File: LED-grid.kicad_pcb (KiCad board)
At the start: 2 copper layers, 75 x 75 mm, 301 parts

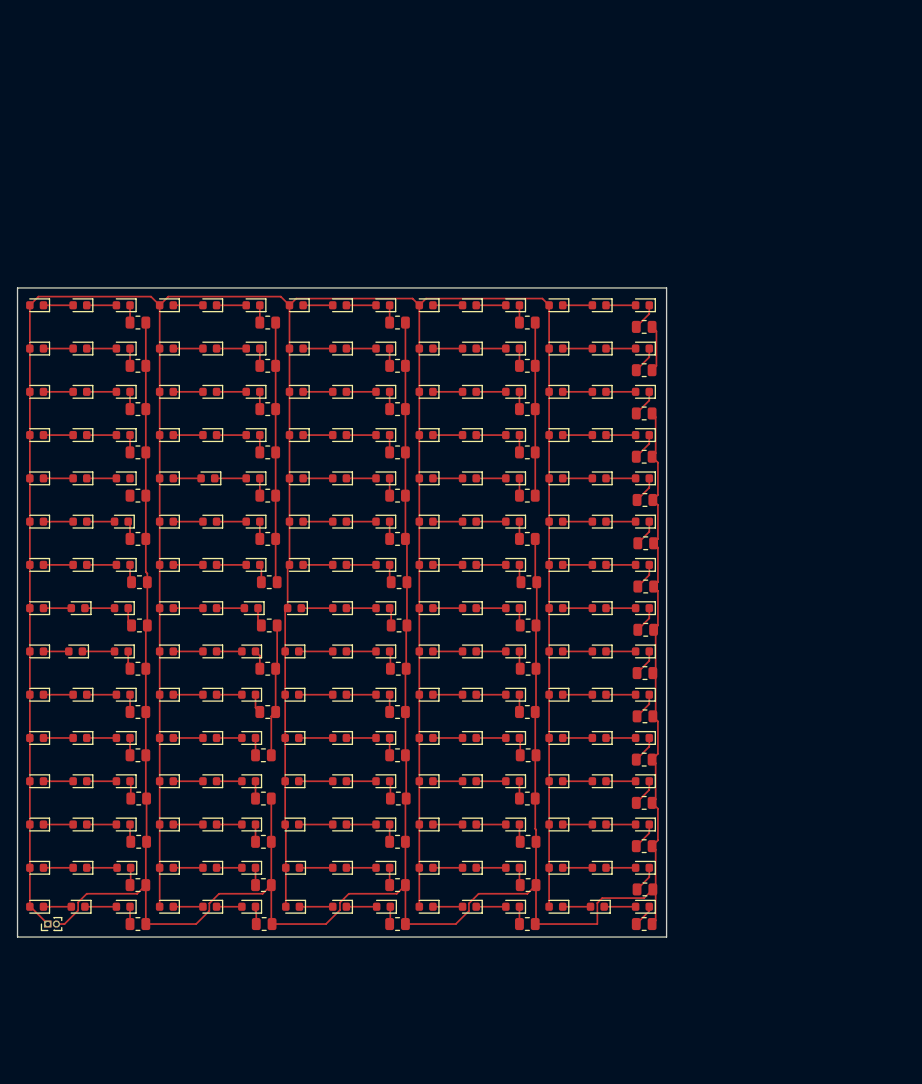
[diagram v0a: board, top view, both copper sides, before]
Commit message: Version 1.0.1 We can now actually control the brightness using a potentiometer
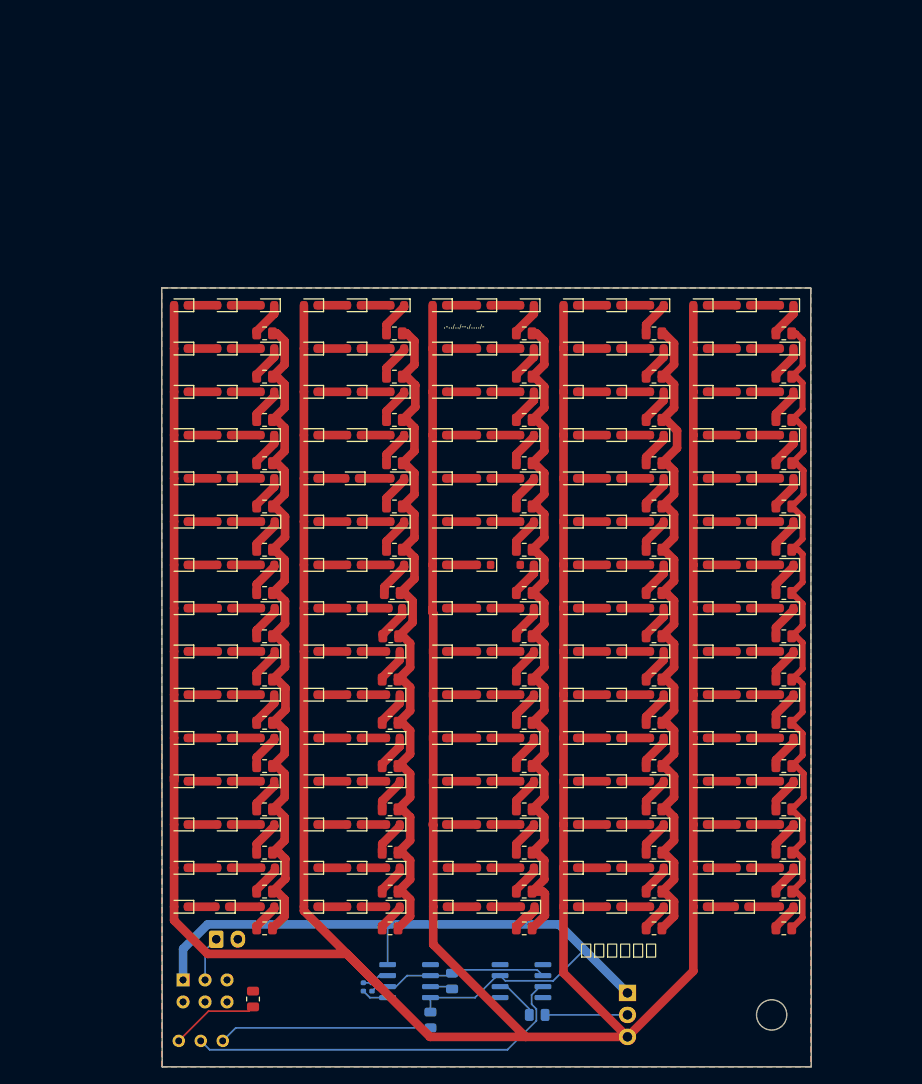
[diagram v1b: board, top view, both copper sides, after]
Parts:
- added C1: 100n, Capacitor_SMD:C_0402_1005Metric, B.Cu at (153.2, 135.8)
- added C2: 100n, Capacitor_SMD:C_0402_1005Metric, B.Cu at (154.2, 135.8)
- added G***: LOGO, SFH11_PBPC_D10_ST_BK:GoblinCatLogo, B.Cu at (139.5, 66.2)
- added G***: LOGO, SFH11_PBPC_D10_ST_BK:PiShockLogo, B.Cu at (190.5, 115.0)
- added Q1: NMOS, Package_TO_SOT_THT:TO-220-3_Horizontal_TabUp, B.Cu at (183.8, 136.5)
- added R76: 1k, Resistor_SMD:R_0805_2012Metric, B.Cu at (163.5, 135.1)
- added R77: 1k, Resistor_SMD:R_0805_2012Metric, B.Cu at (161.0, 139.6)
- added R78: 1k, Resistor_SMD:R_0805_2012Metric, F.Cu at (140.5, 137.2)
- added R79: 1k, Resistor_SMD:R_0805_2012Metric, B.Cu at (173.3, 139.0)
- added RV1: 3296X-1-102LF, Potentiometer_THT:Potentiometer_Bourns_3296X_Horizontal, B.Cu at (137.0, 142.0)
- added SW1: SW_Wuerth_450301014042, Button_Switch_THT:SW_NKK_G1xJP, B.Cu at (132.4, 135.0)
- added U1: NE555D, Package_SO:SOIC-8_3.9x4.9mm_P1.27mm, B.Cu at (158.5, 135.1)
- added U2: LM741, Package_SO:SOIC-8_3.9x4.9mm_P1.27mm, B.Cu at (171.5, 135.1)
- BT1: footprint Connector_PinHeader_1.00mm:PinHeader_1x02_P1.00mm_Vertical -> Connector_JST:JST_EH_B2B-EH-A_1x02_P2.50mm_Vertical; moved to B.Cu
- moved BT1 19.5 mm to (136.2, 130.2), turned to 0 degrees
- moved D122 17.2 mm to (137.2, 97.0)
- moved D202 17.0 mm to (162.1, 122.0)
- moved D217 17.0 mm to (162.1, 126.5)
- moved D127 17.0 mm to (162.0, 97.0)
- moved D142 17.0 mm to (162.0, 102.0)
- moved D157 17.0 mm to (162.0, 107.0)
- moved D172 17.0 mm to (162.0, 112.0)
- moved D187 17.0 mm to (162.0, 117.0)
- moved D107 16.9 mm to (137.2, 92.0)
- moved D108 16.9 mm to (142.2, 92.0)
- moved D123 16.9 mm to (142.2, 97.0)
- moved D78 16.9 mm to (142.2, 82.0)
- moved D112 16.8 mm to (162.0, 92.0)
- moved D111 16.7 mm to (157.0, 92.0)
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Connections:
- BT1 pad 1: VCC -> Net-(BT1-+)
- D1 pad 2: VCC -> LED_PWR
- D10 pad 2: VCC -> LED_PWR
- D100 pad 2: VCC -> LED_PWR
- D103 pad 2: VCC -> LED_PWR
- D106 pad 2: VCC -> LED_PWR
- D109 pad 2: VCC -> LED_PWR
- D112 pad 2: VCC -> LED_PWR
- D115 pad 2: VCC -> LED_PWR
- D118 pad 2: VCC -> LED_PWR
- D121 pad 2: VCC -> LED_PWR
- D124 pad 2: VCC -> LED_PWR
- D127 pad 2: VCC -> LED_PWR
- D13 pad 2: VCC -> LED_PWR
- D130 pad 2: VCC -> LED_PWR
- D133 pad 2: VCC -> LED_PWR
- D136 pad 2: VCC -> LED_PWR
- D139 pad 2: VCC -> LED_PWR
- D142 pad 2: VCC -> LED_PWR
- D145 pad 2: VCC -> LED_PWR
- D148 pad 2: VCC -> LED_PWR
- D151 pad 2: VCC -> LED_PWR
- D154 pad 2: VCC -> LED_PWR
- D157 pad 2: VCC -> LED_PWR
- D16 pad 2: VCC -> LED_PWR
- D160 pad 2: VCC -> LED_PWR
- D163 pad 2: VCC -> LED_PWR
- D166 pad 2: VCC -> LED_PWR
- D169 pad 2: VCC -> LED_PWR
- D172 pad 2: VCC -> LED_PWR
- D175 pad 2: VCC -> LED_PWR
- D178 pad 2: VCC -> LED_PWR
- D181 pad 2: VCC -> LED_PWR
- D184 pad 2: VCC -> LED_PWR
- D187 pad 2: VCC -> LED_PWR
- D19 pad 2: VCC -> LED_PWR
- D190 pad 2: VCC -> LED_PWR
- D193 pad 2: VCC -> LED_PWR
- D196 pad 2: VCC -> LED_PWR
- D199 pad 2: VCC -> LED_PWR
- D202 pad 2: VCC -> LED_PWR
- D205 pad 2: VCC -> LED_PWR
- D208 pad 2: VCC -> LED_PWR
- D211 pad 2: VCC -> LED_PWR
- D214 pad 2: VCC -> LED_PWR
- D217 pad 2: VCC -> LED_PWR
- D22 pad 2: VCC -> LED_PWR
- D220 pad 2: VCC -> LED_PWR
- D223 pad 2: VCC -> LED_PWR
- D25 pad 2: VCC -> LED_PWR
- D28 pad 2: VCC -> LED_PWR
- D31 pad 2: VCC -> LED_PWR
- D34 pad 2: VCC -> LED_PWR
- D37 pad 2: VCC -> LED_PWR
- D4 pad 2: VCC -> LED_PWR
- D40 pad 2: VCC -> LED_PWR
- D43 pad 2: VCC -> LED_PWR
- D46 pad 2: VCC -> LED_PWR
- D49 pad 2: VCC -> LED_PWR
- D52 pad 2: VCC -> LED_PWR
- D55 pad 2: VCC -> LED_PWR
- D58 pad 2: VCC -> LED_PWR
- D61 pad 2: VCC -> LED_PWR
- D64 pad 2: VCC -> LED_PWR
- D67 pad 2: VCC -> LED_PWR
- D7 pad 2: VCC -> LED_PWR
- D70 pad 2: VCC -> LED_PWR
- D73 pad 2: VCC -> LED_PWR
- D76 pad 2: VCC -> LED_PWR
- D79 pad 2: VCC -> LED_PWR
- D82 pad 2: VCC -> LED_PWR
- D85 pad 2: VCC -> LED_PWR
- D88 pad 2: VCC -> LED_PWR
- D91 pad 2: VCC -> LED_PWR
- D94 pad 2: VCC -> LED_PWR
- D97 pad 2: VCC -> LED_PWR
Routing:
- net LED_PWR: track 0.00 -> 476.8 mm
- net VCC: track 413.6 -> 87.4 mm
- net Net-(U2-+): track 0.00 -> 45.5 mm
- net GND: track 414.7 -> 447.0 mm
- net Net-(R77-Pad1): track 0.00 -> 24.6 mm
- net Net-(U1-THR): track 0.00 -> 21.0 mm
- net Net-(R78-Pad2): track 0.00 -> 10.2 mm
- net Net-(Q1-G): track 0.00 -> 9.52 mm
- net Net-(BT1-+): track 0.00 -> 5.24 mm
- net Net-(R79-Pad1): track 0.00 -> 5.14 mm
- net Net-(D63-K): track 0.00 -> 4.09 mm
- net Net-(D98-K): track 3.43 -> 0.00 mm
- net Net-(U1-CV): track 0.00 -> 3.11 mm
- net Net-(U1-Q): track 0.00 -> 2.61 mm
- net Net-(D96-K): track 2.07 -> 4.44 mm
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- added copper zone on B.Cu, net GND
- added copper zone on F.Cu, net GND
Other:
- board size 75 x 75 mm -> 75 x 90 mm
- board text added: ".-../../--./..../-"
- board text added: "A PiShock product"
- board text added: "Designed by:"
- board text added: "FLASHBANG v1.0.1"
- board text added: "GitHub: dorythecat Discord: dorythecat"
- board text added: "Lights, camera, action!"
- board text added: "手が痛かった"

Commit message: Updated PCB
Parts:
- removed BT1: 6V, Connector_JST:JST_EH_B2B-EH-A_1x02_P2.50mm_Vertical
- removed Q1: NMOS, Package_TO_SOT_THT:TO-220-3_Horizontal_TabUp
- removed R35, R36, R37, R38, R39, R40, R41, R42, R43, R44, R45, R46, R47, R48, R49, R50, R51, R52, R53, R54, R55, R56, R57, R58, R59, R60, R61, R62, R63, R64, R65, R66, R67, R68, R69, R70, R71, R72, R73, R74, R75: 120, Resistor_SMD:R_0805_2012Metric
- removed R76, R77, R78, R79: 1k, Resistor_SMD:R_0805_2012Metric
- removed U2: LM741, Package_SO:SOIC-8_3.9x4.9mm_P1.27mm
- added C3: 1u, Capacitor_SMD:C_0603_1608Metric, F.Cu at (171.0, 92.3)
- added C4: 1u, Capacitor_SMD:C_0603_1608Metric, F.Cu at (195.2, 89.3)
- added C5: 1u, Capacitor_SMD:C_0603_1608Metric, F.Cu at (195.2, 92.8)
- added C6: 10n, Capacitor_SMD:C_0603_1608Metric, F.Cu at (198.2, 93.6)
- added C7: 1n, Capacitor_SMD:C_0201_0603Metric, F.Cu at (200.0, 91.6)
- added C8: 2u, Capacitor_SMD:C_0603_1608Metric, F.Cu at (202.8, 90.5)
- added C9: 47n, Capacitor_SMD:C_0201_0603Metric, F.Cu at (201.1, 92.6)
- added D226: LED, LED_SMD:LED_0603_1608Metric, F.Cu at (208.0, 84.8)
- added D227: LED, LED_SMD:LED_0603_1608Metric, F.Cu at (212.5, 84.8)
- added J1: Conn_01x03_Pin, Connector_JST:JST_ZH_B3B-ZR_1x03_P1.50mm_Vertical, B.Cu at (166.8, 91.3)
- added J2: USB_C_Receptacle, Connector_USB:USB_C_Receptacle_Amphenol_12401610E4-2A, F.Cu at (182.8, 93.6)
- added L1: 30u, Inductor_SMD:L_0603_1608Metric, F.Cu at (197.7, 88.6)
- added U3: BQ24052, Package_SON:WSON-10-1EP_2.5x2.5mm_P0.5mm_EP1.2x2mm_ThermalVias, F.Cu at (173.2, 90.1)
- C1, C2: value 100n -> 1u; footprint Capacitor_SMD:C_0402_1005Metric -> Capacitor_SMD:C_0603_1608Metric; moved to F.Cu
- D2: value LED -> D; footprint LED_SMD:LED_0603_1608Metric -> Diode_SMD:D_0603_1608Metric
- G*** (x2): moved to F.Cu
- R1, R2: value 120 -> 5.1k; footprint Resistor_SMD:R_0805_2012Metric -> Resistor_SMD:R_0201_0603Metric
- R10, R11, R12, R13, R14, R15, R16, R17, R18, R19, R20, R21, R22, R23, R24, R25, R26, R27, R28, R29, R30, R31, R32, R33, R34: value 120 -> 20; footprint Resistor_SMD:R_0805_2012Metric -> Resistor_SMD:R_0201_0603Metric
- R3, R4, R6: value 120 -> 1k; footprint Resistor_SMD:R_0805_2012Metric -> Resistor_SMD:R_0201_0603Metric
- R5: value 120 -> 2k; footprint Resistor_SMD:R_0805_2012Metric -> Resistor_SMD:R_0201_0603Metric
- R7, R8: value 120 -> 100; footprint Resistor_SMD:R_0805_2012Metric -> Resistor_SMD:R_0201_0603Metric
- R9: value 120 -> 1.6; footprint Resistor_SMD:R_0805_2012Metric -> Resistor_SMD:R_0201_0603Metric
- RV1: value 3296X-1-102LF -> 1k
- SW1: footprint Button_Switch_THT:SW_NKK_G1xJP -> Button_Switch_THT:SW_Slide-03_Wuerth-WS-SLTV_10x2.5x6.4_P2.54mm
- U1: value NE555D -> TPS923650D2DRLR; footprint Package_SO:SOIC-8_3.9x4.9mm_P1.27mm -> Package_SON:WSON-8-1EP_2x2mm_P0.5mm_EP0.9x1.6mm_ThermalVias; moved to F.Cu
- moved D183 110.4 mm to (203.5, 25.2)
- moved D184 110.1 mm to (208.0, 25.2)
- moved D196 110.1 mm to (208.0, 42.2), turned to 0 degrees
- moved D185 109.8 mm to (212.5, 25.2)
- moved D186 103.8 mm to (212.5, 29.5), turned to 0 degrees
- moved D197 103.8 mm to (203.5, 42.2), turned to 0 degrees
- moved D187 98.9 mm to (208.0, 29.5), turned to 0 degrees
- moved D211 98.6 mm to (208.0, 63.5)
- moved D212 98.4 mm to (212.5, 63.5)
- moved D198 97.2 mm to (203.5, 46.5)
- moved D199 97.0 mm to (208.0, 46.5)
- moved D200 96.7 mm to (212.5, 46.5)
- moved D138 95.5 mm to (199.0, 25.2), turned to 0 degrees
- moved D188 94.8 mm to (203.5, 29.5), turned to 0 degrees
- moved D213 91.7 mm to (212.5, 67.8), turned to 0 degrees
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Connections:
- C1 pad 1: Net-(U1-CV) -> Net-(C1-Pad1)
- C2 pad 1: Net-(U1-THR) -> VBUS
- D1 pad 2: LED_PWR -> BAT
- D10 pad 2: LED_PWR -> Net-(D10-A)
- D100 pad 2: LED_PWR -> Net-(D100-A)
- D102 pad 2: Net-(D101-K) -> LED_PWR
- D103 pad 2: LED_PWR -> Net-(D102-K)
- D106 pad 2: LED_PWR -> Net-(D105-K)
- D109 pad 2: LED_PWR -> Net-(D108-K)
- D111 pad 2: Net-(D110-K) -> LED_PWR
- D112 pad 2: LED_PWR -> Net-(D111-K)
- D115 pad 2: LED_PWR -> Net-(D114-K)
- D118 pad 2: LED_PWR -> Net-(D117-K)
- D12 pad 2: Net-(D11-K) -> LED_PWR
- D120 pad 2: Net-(D119-K) -> LED_PWR
- D121 pad 2: LED_PWR -> Net-(D120-K)
- D124 pad 2: LED_PWR -> Net-(D123-K)
- D127 pad 2: LED_PWR -> Net-(D126-K)
- D129 pad 2: Net-(D128-K) -> LED_PWR
- D13 pad 2: LED_PWR -> Net-(D12-K)
- D130 pad 2: LED_PWR -> Net-(D129-K)
- D133 pad 2: LED_PWR -> Net-(D132-K)
- D136 pad 2: LED_PWR -> Net-(D135-K)
- D138 pad 2: Net-(D137-K) -> LED_PWR
- D139 pad 2: LED_PWR -> Net-(D138-K)
- D142 pad 2: LED_PWR -> Net-(D141-K)
- D145 pad 2: LED_PWR -> Net-(D144-K)
- D147 pad 2: Net-(D146-K) -> LED_PWR
- D148 pad 2: LED_PWR -> Net-(D147-K)
- D151 pad 2: LED_PWR -> Net-(D150-K)
- D154 pad 2: LED_PWR -> Net-(D153-K)
- D156 pad 2: Net-(D155-K) -> LED_PWR
- D157 pad 2: LED_PWR -> Net-(D156-K)
- D16 pad 2: LED_PWR -> Net-(D15-K)
- D160 pad 2: LED_PWR -> Net-(D159-K)
- D163 pad 2: LED_PWR -> Net-(D162-K)
- D165 pad 2: Net-(D164-K) -> LED_PWR
- D166 pad 2: LED_PWR -> Net-(D165-K)
- D169 pad 2: LED_PWR -> Net-(D168-K)
- D172 pad 2: LED_PWR -> Net-(D171-K)
- D174 pad 2: Net-(D173-K) -> LED_PWR
- D175 pad 2: LED_PWR -> Net-(D174-K)
- D178 pad 2: LED_PWR -> Net-(D177-K)
- D181 pad 2: LED_PWR -> Net-(D180-K)
- D183 pad 2: Net-(D182-K) -> LED_PWR
- D184 pad 2: LED_PWR -> Net-(D183-K)
- D187 pad 2: LED_PWR -> Net-(D186-K)
- D19 pad 2: LED_PWR -> Net-(D18-K)
- D190 pad 2: LED_PWR -> Net-(D189-K)
- D192 pad 2: Net-(D191-K) -> LED_PWR
- D193 pad 2: LED_PWR -> Net-(D192-K)
- D196 pad 2: LED_PWR -> Net-(D195-K)
- D199 pad 2: LED_PWR -> Net-(D198-K)
- D2 pad 2: Net-(D1-K) -> Net-(D2-A)
- D201 pad 2: Net-(D200-K) -> LED_PWR
- D202 pad 2: LED_PWR -> Net-(D201-K)
- D205 pad 2: LED_PWR -> Net-(D204-K)
- D208 pad 2: LED_PWR -> Net-(D207-K)
- D21 pad 2: Net-(D20-K) -> LED_PWR
- D210 pad 2: Net-(D209-K) -> LED_PWR
- D211 pad 2: LED_PWR -> Net-(D210-K)
- D214 pad 2: LED_PWR -> Net-(D213-K)
- D217 pad 2: LED_PWR -> Net-(D216-K)
- D219 pad 2: Net-(D218-K) -> LED_PWR
- D22 pad 2: LED_PWR -> Net-(D21-K)
- D220 pad 2: LED_PWR -> Net-(D219-K)
- D223 pad 2: LED_PWR -> Net-(D222-K)
- D25 pad 2: LED_PWR -> Net-(D24-K)
- D28 pad 2: LED_PWR -> Net-(D27-K)
- D3 pad 2: Net-(D2-K) -> LED_PWR
- D30 pad 2: Net-(D29-K) -> LED_PWR
- D31 pad 2: LED_PWR -> Net-(D30-K)
- D34 pad 2: LED_PWR -> Net-(D33-K)
- D37 pad 2: LED_PWR -> Net-(D36-K)
- D39 pad 2: Net-(D38-K) -> LED_PWR
- D4 pad 2: LED_PWR -> Net-(D3-K)
- D40 pad 2: LED_PWR -> Net-(D39-K)
- D43 pad 2: LED_PWR -> Net-(D42-K)
- D46 pad 2: LED_PWR -> Net-(D45-K)
- D48 pad 2: Net-(D47-K) -> LED_PWR
- D49 pad 2: LED_PWR -> Net-(D48-K)
- D52 pad 2: LED_PWR -> Net-(D51-K)
- D55 pad 2: LED_PWR -> Net-(D54-K)
- D57 pad 2: Net-(D56-K) -> LED_PWR
- D58 pad 2: LED_PWR -> Net-(D57-K)
- D61 pad 2: LED_PWR -> Net-(D60-K)
- D64 pad 2: LED_PWR -> Net-(D63-K)
- D66 pad 2: Net-(D65-K) -> LED_PWR
- D67 pad 2: LED_PWR -> Net-(D66-K)
- D7 pad 2: LED_PWR -> Net-(D6-K)
- D70 pad 2: LED_PWR -> Net-(D69-K)
- D73 pad 2: LED_PWR -> Net-(D72-K)
- D75 pad 2: Net-(D74-K) -> LED_PWR
- D76 pad 2: LED_PWR -> Net-(D75-K)
- D79 pad 2: LED_PWR -> Net-(D78-K)
- D82 pad 2: LED_PWR -> Net-(D81-K)
- D84 pad 2: Net-(D83-K) -> LED_PWR
- D85 pad 2: LED_PWR -> Net-(D84-K)
- D88 pad 2: LED_PWR -> Net-(D87-K)
- D9 pad 1: Net-(D9-K) -> Net-(D10-A)
- D91 pad 2: LED_PWR -> Net-(D90-K)
- D93 pad 2: Net-(D92-K) -> LED_PWR
- D94 pad 2: LED_PWR -> Net-(D93-K)
- D97 pad 2: LED_PWR -> Net-(D96-K)
- D99 pad 1: Net-(D99-K) -> Net-(D100-A)
- R1 pad 1: Net-(D3-K) -> Net-(J2-CC1)
- R10 pad 1: Net-(D30-K) -> Net-(D11-K)
- R11 pad 1: Net-(D33-K) -> Net-(D20-K)
- R12 pad 1: Net-(D36-K) -> Net-(D29-K)
- R13 pad 1: Net-(D39-K) -> Net-(D38-K)
- R14 pad 1: Net-(D42-K) -> Net-(D47-K)
- R15 pad 1: Net-(D45-K) -> Net-(D56-K)
- R16 pad 1: Net-(D48-K) -> Net-(D65-K)
- R17 pad 1: Net-(D51-K) -> Net-(D74-K)
- R18 pad 1: Net-(D54-K) -> Net-(D83-K)
- R19 pad 1: Net-(D57-K) -> Net-(D92-K)
- R2 pad 1: Net-(D6-K) -> Net-(J2-CC2)
- R20 pad 1: Net-(D60-K) -> Net-(D101-K)
- R21 pad 1: Net-(D63-K) -> Net-(D110-K)
- R22 pad 1: Net-(D66-K) -> Net-(D119-K)
- R23 pad 1: Net-(D69-K) -> Net-(D128-K)
- R24 pad 1: Net-(D72-K) -> Net-(D137-K)
- R25 pad 1: Net-(D75-K) -> Net-(D146-K)
- R26 pad 1: Net-(D78-K) -> Net-(D155-K)
- R27 pad 1: Net-(D81-K) -> Net-(D164-K)
- R28 pad 1: Net-(D84-K) -> Net-(D173-K)
- R29 pad 1: Net-(D87-K) -> Net-(D182-K)
- R3 pad 1: Net-(D9-K) -> Net-(J2-SHIELD)
- R3 pad 2: GND -> Net-(C1-Pad1)
- R30 pad 1: Net-(D90-K) -> Net-(D191-K)
- R31 pad 1: Net-(D93-K) -> Net-(D200-K)
- R32 pad 1: Net-(D96-K) -> Net-(D209-K)
- R33 pad 1: Net-(D99-K) -> Net-(D218-K)
- R34 pad 1: Net-(D102-K) -> Net-(D227-K)
- R4 pad 1: Net-(D12-K) -> GND
- R4 pad 2: GND -> Net-(U3-ISET)
- R5 pad 1: Net-(D15-K) -> GND
- R5 pad 2: GND -> Net-(U3-PRE-TERM)
- R6 pad 1: Net-(D18-K) -> Net-(U3-OUT)
- R6 pad 2: GND -> BAT
- R7 pad 1: Net-(D21-K) -> Net-(U1-COMP)
- R7 pad 2: GND -> Net-(C6-Pad1)
- R8 pad 1: Net-(D24-K) -> Net-(U1-CSN)
- R8 pad 2: GND -> LED_PWR
- R9 pad 1: Net-(D27-K) -> Net-(D2-K)
- R9 pad 2: GND -> LED_PWR
- RV1 pad 1: Net-(R77-Pad1) -> VCC
- RV1 pad 2: Net-(U2-+) -> Net-(U1-DIM)
- RV1 pad 3: Net-(R78-Pad2) -> GND
- SW1 pad 2: Net-(BT1-+) -> GND
- SW1 pad 3: GND -> BAT
- U1 pad 2: Net-(U1-THR) -> VCC
- U1 pad 3: Net-(U1-Q) -> Net-(U1-DIM)
- U1 pad 4: VCC -> Net-(U1-VCC)
- U1 pad 5: Net-(U1-CV) -> Net-(U1-COMP)
- U1 pad 6: Net-(U1-THR) -> Net-(U1-CSN)
- U1 pad 7: GND -> Net-(D2-K)
- U1 pad 8: VCC -> Net-(D2-A)
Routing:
- net LED_PWR: track 476.8 -> 198.7 mm, vias 0 -> 2
- net GND: track 447.0 -> 202.3 mm
- net VCC: track 87.4 -> 40.6 mm
- net Net-(U2-+): track 45.5 -> 0.00 mm
- net Net-(R77-Pad1): track 24.6 -> 0.00 mm
- net Net-(J2-SHIELD): track 0.00 -> 22.2 mm
- net Net-(U1-THR): track 21.0 -> 0.00 mm
- net VBUS: track 0.00 -> 20.0 mm, vias 0 -> 2
- net USB_D-: track 0.00 -> 15.7 mm, vias 0 -> 2
- net USB_D+: track 0.00 -> 11.0 mm
- net BAT: track 0.00 -> 10.3 mm
- net Net-(R78-Pad2): track 10.2 -> 0.00 mm
- net Net-(Q1-G): track 9.52 -> 0.00 mm
- net Net-(J2-CC2): track 0.00 -> 6.34 mm
- net Net-(U1-DIM): track 0.00 -> 5.86 mm
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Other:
- board size 75 x 90 mm -> 67 x 74 mm
- board text removed: ".-../../--./..../-"
- board text removed: "A PiShock product"
- board text removed: "Designed by:"
- board text removed: "FLASHBANG v1.0.1"
- board text removed: "GitHub: dorythecat Discord: dorythecat"
- board text removed: "Lights, camera, action!"
- board text removed: "R20"
- board text removed: "手が痛かった"

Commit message: Final touches to PCB
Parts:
- RV1: footprint Potentiometer_THT:Potentiometer_Bourns_3296X_Horizontal -> Potentiometer_THT:Potentiometer_Bourns_3386P_Vertical
- moved C6 3.13 mm to (201.3, 93.0)
- moved C7 3.13 mm to (203.1, 91.1)
- moved C8 3.13 mm to (205.8, 90.0)
- moved D2 3.13 mm to (203.3, 88.8)
- moved R9 3.13 mm to (204.6, 90.1)
- moved C4 3.13 mm to (198.3, 88.8)
- moved C5 3.13 mm to (198.3, 92.3)
- moved C9 3.13 mm to (204.2, 92.0)
- moved L1 3.13 mm to (200.8, 88.0)
- moved R7 3.13 mm to (202.0, 91.8)
- moved R8 3.13 mm to (204.2, 91.2)
- moved U1 3.13 mm to (200.8, 90.0)
- moved G*** 2.30 mm to (210.8, 93.2)
- moved RV1 2.04 mm to (191.4, 92.2)
- moved G*** 1.12 mm to (155.0, 92.0)
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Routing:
- net GND: track 202.3 -> 191.1 mm
- net LED_PWR: track 198.7 -> 201.9 mm
- net VCC: track 40.6 -> 41.3 mm
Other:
- board text added: ".-.. .. --. .... -"
- board text added: "3.5W of light, in a portable format"
- board text added: "6D616B656C6D76656E6F74776172"
- board text added: "A PiShock Product https://pishock.com"
- board text added: "Be gay, do crime"
- board text added: "Designed by Dory"
- board text added: "Do not eat the board. I know it looks tasty, but. Just trust me."
- board text added: "FLASHBANG v1.0.2"
- board text added: "Gluten-free electronics Keep away from protogens"
- board text added: "https://github.com/dorythecat"
- board text added: "xkcd.com/1603"
- board text added: "銅が多すぎる"
